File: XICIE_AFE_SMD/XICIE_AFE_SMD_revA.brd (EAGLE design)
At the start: 101 x 60.4 mm, 32 parts, among them IC1 LM324D, IC2 CY8C4245T, IC3 AAT1217, J1 22-27-2021-02, Q1 MOSFET-NCHANNELBSS123LT1G, Q2 MOSFET-NCHANNELBSS123LT1G

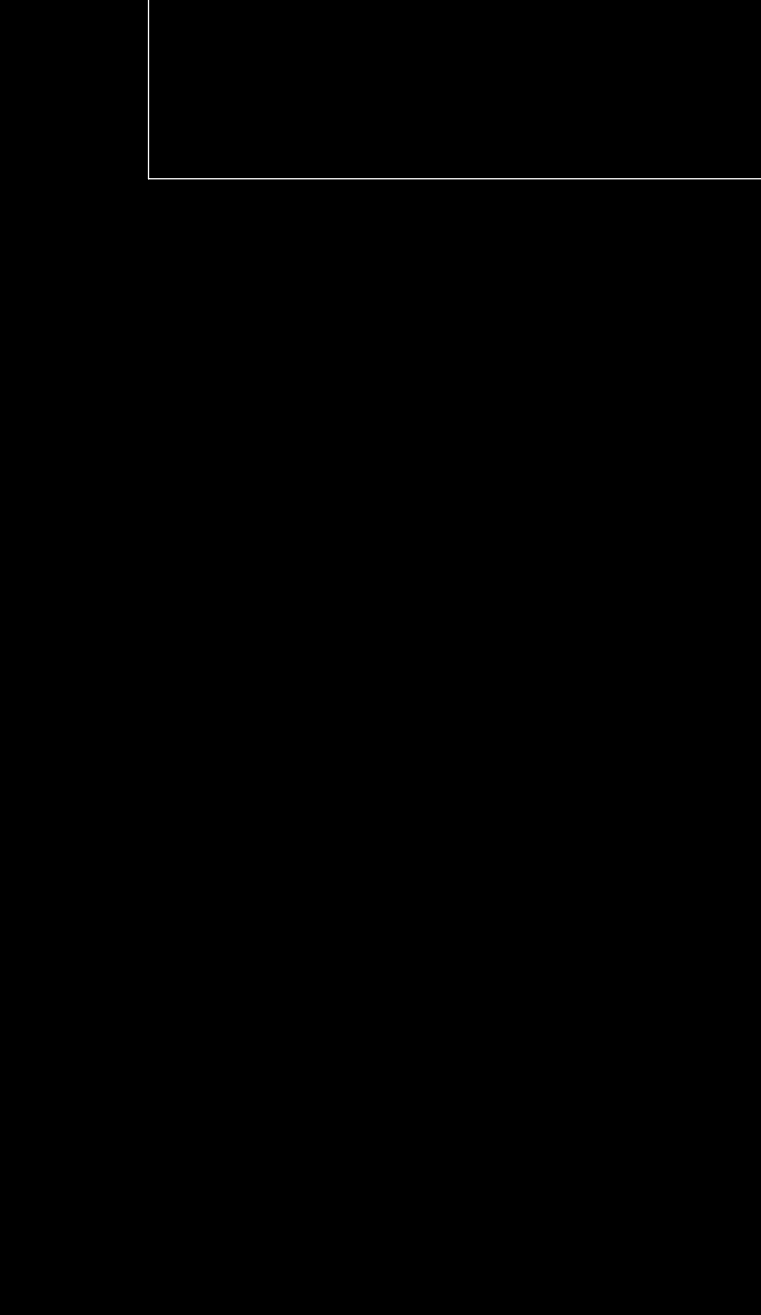
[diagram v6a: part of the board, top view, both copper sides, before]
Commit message: Added all components and connections
Still in doubt if BUZZ driver will use a resistor,
and if TIA should have a capacitor.
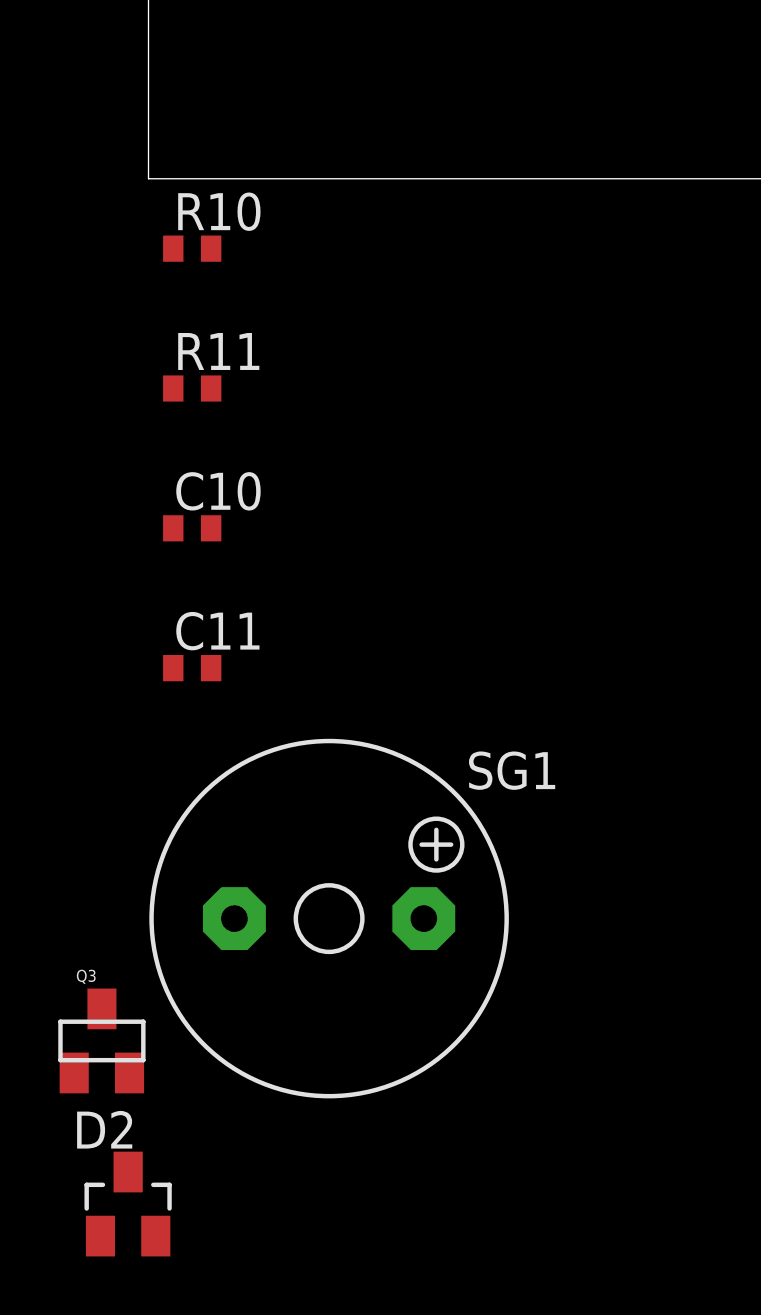
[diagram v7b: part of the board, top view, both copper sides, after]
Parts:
- added C10, C11: 0.1 uF, rcl:C0402
- added D2: (no value), diode:SOT23
- added Q3: MOSFET-NCHANNELBSS123LT1G, SparkFun-DiscreteSemi:SOT23
- added R10, R11: 2.2 k, rcl:R0402
- added SG1: F/QMX, buzzer:F/QMX
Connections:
- removed net V2.1: C9.1, U$2.P27
- new net BUZZ: IC2.27, Q3.1
- new net N$13: D2.1, Q3.3, SG1.-
- net +3V3: now also C11.1, D2.3, SG1.+
- net GND: now also C10.2, C11.2, Q3.2
- net SCL: now also IC2.20, R10.1
- net SDA: now also IC2.21, R11.1
- net VCC: now also C10.1, C9.1, R10.2, R11.2, U$2.P27
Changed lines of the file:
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@@
 <?xml version="1.0" encoding="utf-8"?>
 <!DOCTYPE eagle SYSTEM "eagle.dtd">
-<eagle version="6.4">
+<eagle version="6.5.0">
 <drawing>
 <settings>
@@
 <element name="R9" library="rcl" package="R0603" value="150 k" x="45.85" y="49.5" rot="R270"/>
 <element name="U$4" library="juliano" package="DFN10" value="MMA7660FC" x="55.6" y="49.9" rot="MR0"/>
+<element name="R10" library="rcl" package="R0402" value="2.2 k" x="3.9" y="17.4"/>
+<element name="R11" library="rcl" package="R0402" value="2.2 k" x="3.9" y="12.6"/>
+<element name="C10" library="rcl" package="C0402" value="0.1 uF" x="3.9" y="7.8"/>
+<element name="C11" library="rcl" package="C0402" value="0.1 uF" x="3.9" y="3"/>
+<element name="SG1" library="buzzer" package="F/QMX" value="F/QMX" x="8.6" y="-5.6">
+<attribute name="OC_NEWARK" value="unknown" x="8.6" y="-5.6" size="1.778" layer="27" display="off"/>
+<attribute name="MPN" value="" x="8.6" y="-5.6" size="1.778" layer="27" display="off"/>
+<attribute name="MF" value="" x="8.6" y="-5.6" size="1.778" layer="27" display="off"/>
+<attribute name="OC_FARNELL" value="unknown" x="8.6" y="-5.6" size="1.778" layer="27" display="off"/>
+</element>
+<element name="Q3" library="SparkFun-DiscreteSemi" package="SOT23" value="MOSFET-NCHANNELBSS123LT1G" x="0.8" y="-9.8">
+<attribute name="PROD_ID" value="TRANS-08345" x="0.8" y="-9.8" size="1.778" layer="27" display="off"/>
+</element>
+<element name="D2" library="diode" package="SOT23" value="" x="1.7" y="-15.4"/>
 </elements>
 <signals>
@@
 <contactref element="IC2" pad="19"/>
 <contactref element="U$4" pad="P9"/>
+<contactref element="R10" pad="2"/>
+<contactref element="R11" pad="2"/>
+<contactref element="U$2" pad="P27"/>
+<contactref element="C9" pad="1"/>
+<contactref element="C10" pad="1"/>
 <wire x1="50.11" y1="63.95" x2="51.91" y2="65.75" width="0" layer="19" extent="16-16"/>
 <wire x1="54.31" y1="54.15" x2="50.11" y2="63.95" width="0" layer="19" extent="16-16"/>
@@
 <wire x1="26" y1="56.65" x2="26" y2="55.25" width="0" layer="19" extent="16-16"/>
 <wire x1="20.65" y1="57.05" x2="26" y2="56.65" width="0" layer="19" extent="1-16"/>
+<wire x1="20.15" y1="63.9" x2="20.65" y2="57.05" width="0" layer="19" extent="1-1"/>
+<wire x1="26" y1="67.85" x2="20.15" y2="63.9" width="0" layer="19" extent="1-16"/>
+<wire x1="4.55" y1="17.4" x2="20.65" y2="57.05" width="0" layer="19" extent="1-1"/>
+<wire x1="4.55" y1="12.6" x2="4.55" y2="17.4" width="0" layer="19" extent="1-1"/>
+<wire x1="3.25" y1="7.8" x2="4.55" y2="12.6" width="0" layer="19" extent="1-1"/>
 </signal>
 <signal name="GND" class="1">
@@
 <contactref element="U$4" pad="P1"/>
 <contactref element="U$4" pad="P8"/>
+<contactref element="C10" pad="2"/>
+<contactref element="C11" pad="2"/>
+<contactref element="Q3" pad="2"/>
 <wire x1="61.71" y1="56.75" x2="61.71" y2="63.95" width="0" layer="19" extent="16-16"/>
 <wire x1="56.7" y1="55.18" x2="61.71" y2="56.75" width="0" layer="19" extent="1-16"/>
@@
 <wire x1="26" y1="54.55" x2="26" y2="55.95" width="0" layer="19" extent="16-16"/>
 <wire x1="26" y1="49.65" x2="26" y2="54.55" width="0" layer="19" extent="16-16"/>
+<wire x1="4.55" y1="7.8" x2="26" y2="49.65" width="0" layer="19" extent="1-16"/>
+<wire x1="4.55" y1="3" x2="4.55" y2="7.8" width="0" layer="19" extent="1-1"/>
+<wire x1="1.75" y1="-10.9" x2="4.55" y2="3" width="0" layer="19" extent="1-1"/>
 </signal>
 <signal name="SENSOROUT">
@@
 <signal name="N.C.">
 <contactref element="U$2" pad="P7"/>
-</signal>
-<signal name="V2.1">
-<contactref element="C9" pad="1"/>
-<contactref element="U$2" pad="P27"/>
-<wire x1="20.15" y1="63.9" x2="26" y2="67.85" width="0" layer="19" extent="1-16"/>
 </signal>
 <signal name="VCC_DISPLAY" class="2">
@@
 <vertex x="43.6" y="53.05"/>
 </polygon>
+<contactref element="C11" pad="1"/>
+<contactref element="D2" pad="3"/>
+<contactref element="SG1" pad="+"/>
 <wire x1="55.99" y1="62.58" x2="57.39" y2="62.58" width="0" layer="19" extent="1-1"/>
 <wire x1="56.7" y1="60.38" x2="57.39" y2="62.58" width="0" layer="19" extent="1-1"/>
@@
 <wire x1="26" y1="53.15" x2="33.9" y2="56.75" width="0" layer="19" extent="1-16"/>
 <wire x1="55.6" y1="51.14" x2="56.7" y2="60.38" width="0" layer="19" extent="1-16"/>
+<wire x1="3.25" y1="3" x2="26" y2="53.15" width="0" layer="19" extent="1-16"/>
+<wire x1="11.8512" y1="-5.6" x2="3.25" y2="3" width="0" layer="19" extent="1-1"/>
+<wire x1="1.7" y1="-14.3" x2="11.8512" y2="-5.6" width="0" layer="19" extent="1-1"/>
 </signal>
 <signal name="N$14">
@@
 <contactref element="U$2" pad="P19"/>
 <contactref element="U$2" pad="P20"/>
-<wire x1="26" y1="62.25" x2="56.1" y2="48.66" width="0" layer="19" extent="16-16"/>
+<contactref element="R11" pad="1"/>
+<contactref element="IC2" pad="21"/>
+<wire x1="52.71" y1="54.15" x2="56.1" y2="48.66" width="0" layer="19" extent="16-16"/>
+<wire x1="26" y1="62.25" x2="52.71" y2="54.15" width="0" layer="19" extent="16-16"/>
 <wire x1="26" y1="62.95" x2="26" y2="62.25" width="0" layer="19" extent="16-16"/>
+<wire x1="3.25" y1="12.6" x2="26" y2="62.25" width="0" layer="19" extent="1-16"/>
 </signal>
 <signal name="SCL">
 <contactref element="U$4" pad="P6"/>
 <contactref element="U$2" pad="P18"/>
-<wire x1="26" y1="61.55" x2="56.6" y2="48.66" width="0" layer="19" extent="16-16"/>
+<contactref element="R10" pad="1"/>
+<contactref element="IC2" pad="20"/>
+<wire x1="56.6" y1="48.66" x2="53.51" y2="54.15" width="0" layer="19" extent="16-16"/>
+<wire x1="26" y1="61.55" x2="53.51" y2="54.15" width="0" layer="19" extent="16-16"/>
+<wire x1="3.25" y1="17.4" x2="26" y2="61.55" width="0" layer="19" extent="1-16"/>
+</signal>
+<signal name="N$13">
+<contactref element="Q3" pad="3"/>
+<contactref element="SG1" pad="-"/>
+<contactref element="D2" pad="1"/>
+<wire x1="0.8" y1="-8.7" x2="0.75" y2="-16.5" width="0" layer="19" extent="1-1"/>
+<wire x1="5.3488" y1="-5.6" x2="0.8" y2="-8.7" width="0" layer="19" extent="1-1"/>
+</signal>
+<signal name="BUZZ">
+<contactref element="IC2" pad="27"/>
+<contactref element="Q3" pad="1"/>
+<wire x1="-0.15" y1="-10.9" x2="50.11" y2="59.15" width="0" layer="19" extent="1-16"/>
 </signal>
 </signals>

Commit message: Finished layout for first proposal
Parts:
- moved D2 98.5 mm to (51.9, 69.3), turned to 180 degrees
- moved Q3 97.7 mm to (57.2, 70.0), turned to 90 degrees
- moved SG1 85.1 mm to (44.0, 71.8), turned to 180 degrees
- moved C11 73.3 mm to (59.7, 50.6), flipped to the bottom, turned to 270 degrees
- moved C10 65.1 mm to (52.8, 50.8), flipped to the bottom, turned to 270 degrees
- moved R11 48.9 mm to (35.2, 50.2), flipped to the bottom, turned to 90 degrees
- moved R10 44.2 mm to (33.5, 50.2), flipped to the bottom, turned to 90 degrees
- moved R5 16.0 mm to (32.5, 68.5), turned to 90 degrees
- moved C6 13.4 mm to (27.8, 50.6), turned to 270 degrees
- moved C8 12.2 mm to (27.7, 68.5), turned to 90 degrees
- moved C7 11.4 mm to (31.9, 56.3)
- moved C9 10.0 mm to (29.9, 68.5), turned to 90 degrees
- moved C5 6.71 mm to (30.1, 50.6)
- moved R9 4.59 mm to (41.4, 50.4), flipped to the bottom, turned to 90 degrees
- moved U$3 3.37 mm to (37.8, 50.9), flipped to the bottom
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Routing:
- net SDA: track 0.00 -> 55.9 mm, vias 0 -> 3
- net SCL: track 0.00 -> 55.4 mm
- net VREF: track 0.00 -> 24.6 mm, vias 0 -> 1
- net GND: track 0.00 -> 23.6 mm, vias 0 -> 2
- net VCC: track 0.00 -> 21.5 mm, vias 0 -> 5
- net BUZZ: track 0.00 -> 14.7 mm, vias 0 -> 1
- net N$4: track 0.00 -> 14.7 mm
- net N$13: track 0.00 -> 10.6 mm
- net IR: track 0.00 -> 10.1 mm, vias 0 -> 1
- net SENSOROUT: track 0.00 -> 9.02 mm, vias 0 -> 1
- net N$3: track 0.00 -> 8.82 mm
- net +3V3: track 0.00 -> 8.78 mm, vias 0 -> 3
- net N$9: track 0.00 -> 7.87 mm
- net C1N: track 0.00 -> 7.75 mm, vias 0 -> 1
- net N$1: track 0.00 -> 7.72 mm
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- added copper zone on layer 16, net +3V3
- added copper zone on layer 16, net VCC
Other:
- board size 101 x 60.4 mm -> 43.2 x 34 mm
